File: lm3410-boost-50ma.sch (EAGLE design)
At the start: 10 parts

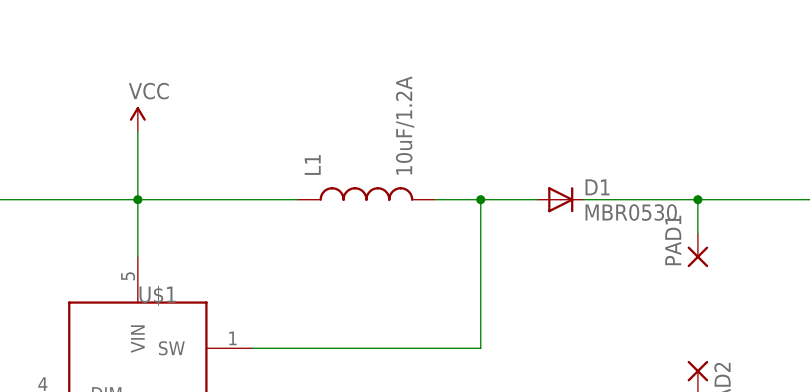
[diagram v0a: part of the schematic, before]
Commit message: Updating layout for lm3410 breakout board
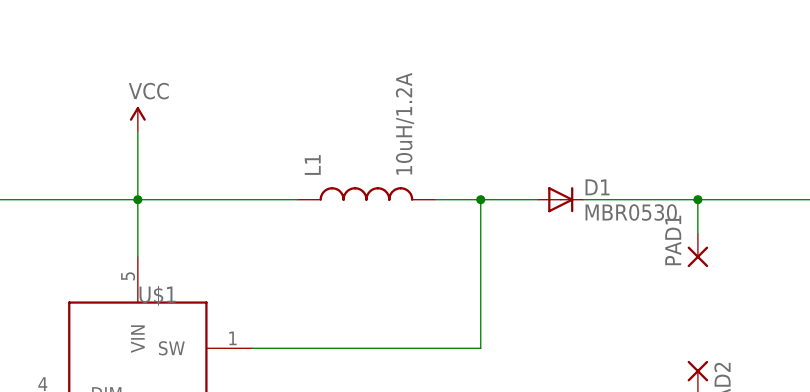
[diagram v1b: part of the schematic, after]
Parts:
- L1: value 10uF/1.2A -> 10uH/1.2A; device SparkFun-Passives:INDUCTORCR75 -> SparkFun-Passives:INDUCTOR1210
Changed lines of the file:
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@@
 <?xml version="1.0" encoding="utf-8"?>
 <!DOCTYPE eagle SYSTEM "eagle.dtd">
-<eagle version="6.4">
+<eagle version="7.0.0">
 <drawing>
 <settings>
@@
 <grid distance="0.05" unitdist="inch" unit="inch" style="lines" multiple="1" display="yes" altdistance="0.005" altunitdist="inch" altunit="inch"/>
 <layers>
-<layer number="1" name="Top" color="4" fill="1" visible="no" active="no"/>
-<layer number="16" name="Bottom" color="1" fill="1" visible="no" active="no"/>
-<layer number="17" name="Pads" color="2" fill="1" visible="no" active="no"/>
-<layer number="18" name="Vias" color="2" fill="1" visible="no" active="no"/>
-<layer number="19" name="Unrouted" color="6" fill="1" visible="no" active="no"/>
-<layer number="20" name="Dimension" color="15" fill="1" visible="no" active="no"/>
-<layer number="21" name="tPlace" color="16" fill="1" visible="no" active="no"/>
-<layer number="22" name="bPlace" color="14" fill="1" visible="no" active="no"/>
-<layer number="23" name="tOrigins" color="15" fill="1" visible="no" active="no"/>
-<layer number="24" name="bOrigins" color="15" fill="1" visible="no" active="no"/>
-<layer number="25" name="tNames" color="7" fill="1" visible="no" active="no"/>
-<layer number="26" name="bNames" color="7" fill="1" visible="no" active="no"/>
-<layer number="27" name="tValues" color="7" fill="1" visible="no" active="no"/>
-<layer number="28" name="bValues" color="7" fill="1" visible="no" active="no"/>
+<layer number="1" name="Top" color="4" fill="1" visible="yes" active="no"/>
+<layer number="16" name="Bottom" color="1" fill="1" visible="yes" active="no"/>
+<layer number="17" name="Pads" color="2" fill="1" visible="yes" active="no"/>
+<layer number="18" name="Vias" color="2" fill="1" visible="yes" active="no"/>
+<layer number="19" name="Unrouted" color="6" fill="1" visible="yes" active="no"/>
+<layer number="20" name="Dimension" color="15" fill="1" visible="yes" active="no"/>
+<layer number="21" name="tPlace" color="16" fill="1" visible="yes" active="no"/>
+<layer number="22" name="bPlace" color="14" fill="1" visible="yes" active="no"/>
+<layer number="23" name="tOrigins" color="15" fill="1" visible="yes" active="no"/>
+<layer number="24" name="bOrigins" color="15" fill="1" visible="yes" active="no"/>
+<layer number="25" name="tNames" color="7" fill="1" visible="yes" active="no"/>
+<layer number="26" name="bNames" color="7" fill="1" visible="yes" active="no"/>
+<layer number="27" name="tValues" color="7" fill="1" visible="yes" active="no"/>
+<layer number="28" name="bValues" color="7" fill="1" visible="yes" active="no"/>
 <layer number="29" name="tStop" color="7" fill="3" visible="no" active="no"/>
 <layer number="30" name="bStop" color="7" fill="6" visible="no" active="no"/>
@@
 <layer number="35" name="tGlue" color="7" fill="4" visible="no" active="no"/>
 <layer number="36" name="bGlue" color="7" fill="5" visible="no" active="no"/>
-<layer number="37" name="tTest" color="7" fill="1" visible="no" active="no"/>
-<layer number="38" name="bTest" color="7" fill="1" visible="no" active="no"/>
+<layer number="37" name="tTest" color="7" fill="1" visible="yes" active="no"/>
+<layer number="38" name="bTest" color="7" fill="1" visible="yes" active="no"/>
 <layer number="39" name="tKeepout" color="4" fill="11" visible="no" active="no"/>
 <layer number="40" name="bKeepout" color="1" fill="11" visible="no" active="no"/>
@@
 <layer number="44" name="Drills" color="7" fill="1" visible="no" active="no"/>
 <layer number="45" name="Holes" color="7" fill="1" visible="no" active="no"/>
-<layer number="46" name="Milling" color="3" fill="1" visible="no" active="no"/>
-<layer number="47" name="Measures" color="7" fill="1" visible="no" active="no"/>
-<layer number="48" name="Document" color="7" fill="1" visible="no" active="no"/>
-<layer number="49" name="Reference" color="7" fill="1" visible="no" active="no"/>
-<layer number="50" name="dxf" color="7" fill="1" visible="no" active="no"/>
-<layer number="51" name="tDocu" color="6" fill="1" visible="no" active="no"/>
-<layer number="52" name="bDocu" color="7" fill="1" visible="no" active="no"/>
-<layer number="53" name="tGND_GNDA" color="7" fill="9" visible="no" active="no"/>
-<layer number="54" name="bGND_GNDA" color="1" fill="9" visible="no" active="no"/>
-<layer number="56" name="wert" color="7" fill="1" visible="no" active="no"/>
+<layer number="46" name="Milling" color="3" fill="1" visible="yes" active="no"/>
+<layer number="47" name="Measures" color="7" fill="1" visible="yes" active="no"/>
+<layer number="48" name="Document" color="7" fill="1" visible="yes" active="no"/>
+<layer number="49" name="Reference" color="7" fill="1" visible="yes" active="no"/>
+<layer number="50" name="dxf" color="7" fill="1" visible="yes" active="no"/>
+<layer number="51" name="tDocu" color="6" fill="1" visible="yes" active="no"/>
+<layer number="52" name="bDocu" color="7" fill="1" visible="yes" active="no"/>
+<layer number="53" name="tGND_GNDA" color="7" fill="9" visible="yes" active="no"/>
+<layer number="54" name="bGND_GNDA" color="1" fill="9" visible="yes" active="no"/>
+<layer number="56" name="wert" color="7" fill="1" visible="yes" active="no"/>
 <layer number="91" name="Nets" color="2" fill="1" visible="yes" active="yes"/>
 <layer number="92" name="Busses" color="1" fill="1" visible="yes" active="yes"/>
@@
 <part name="U$1" library="Synapseware" deviceset="LM3410" device="-SOT-23-5"/>
 <part name="D1" library="diode" deviceset="MBR0520LT" device="" value="MBR0530"/>
-<part name="L1" library="SparkFun-Passives" deviceset="INDUCTOR" device="CR75" value="10uF/1.2A"/>
+<part name="L1" library="SparkFun-Passives" deviceset="INDUCTOR" device="1210" value="10uH/1.2A"/>
 <part name="R1" library="SparkFun-Resistors" deviceset="RESISTOR" device="1206" value="4"/>
 <part name="C2" library="SparkFun-Passives" deviceset="CAP" device="1206" value="2.2uF/25v"/>
